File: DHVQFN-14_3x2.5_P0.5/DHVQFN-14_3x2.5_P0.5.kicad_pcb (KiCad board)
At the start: 2 copper layers, 20.3 x 22.9 mm, 6 parts, among them J101 Conn_01x09, J102 Conn_01x09, J103 Conn_01x12, J104 Conn_01x09, U101 DHVQFN-14

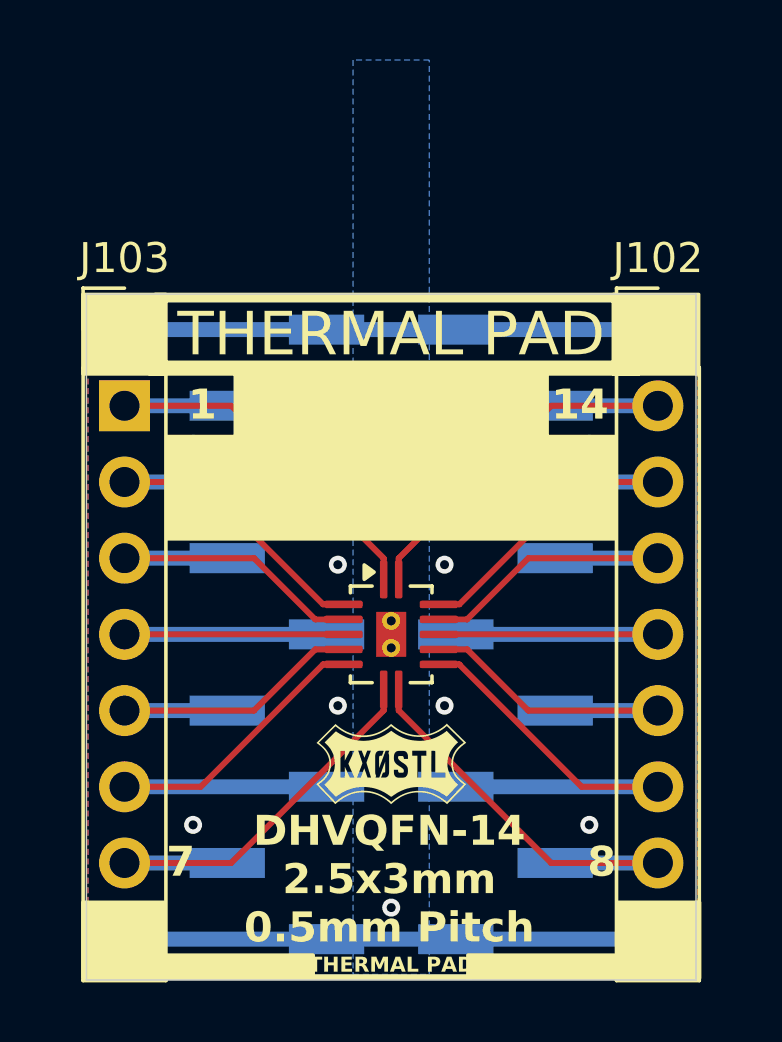
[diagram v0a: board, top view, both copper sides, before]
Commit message: Created SMDIP-16, QFP-48, QFP-32, QFN-80, QFN-68, QFN-64, QFN-60, QFN-56, QFN-48, QFN-36, QFN-28, QFN-20, QFP-32, QFP-48
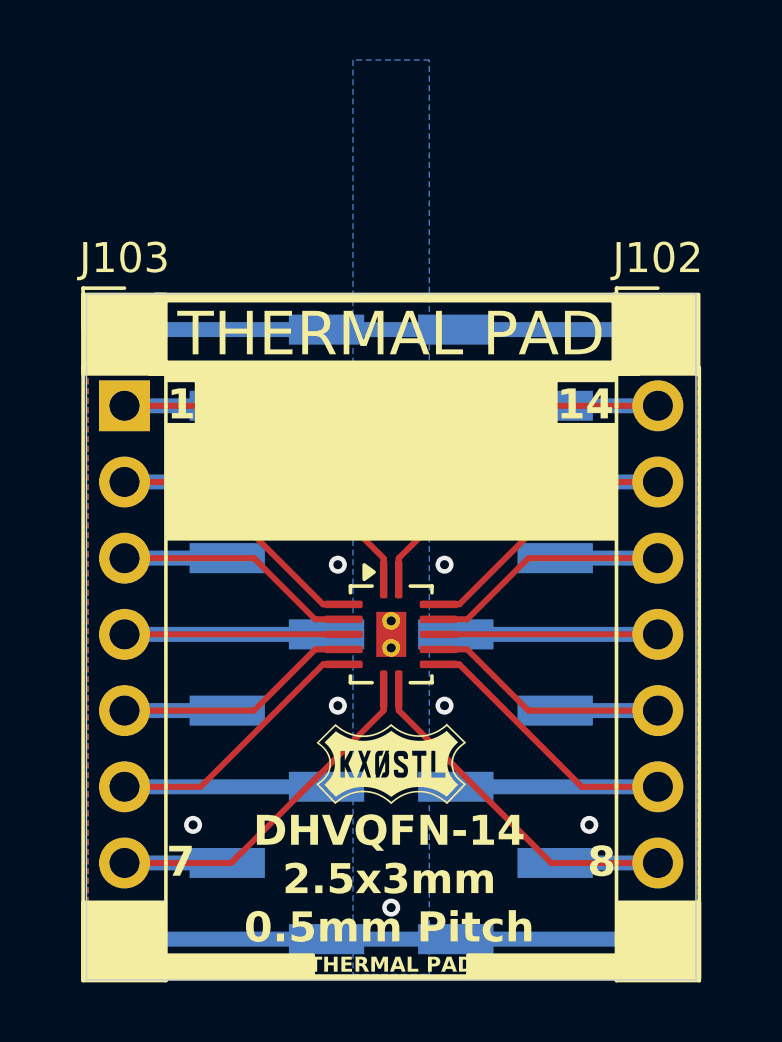
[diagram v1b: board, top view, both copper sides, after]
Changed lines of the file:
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@@
+	)
+	(gr_rect
+		(start 125.659 102.410557)
+		(end 140.533 102.795957)
+		(stroke
+			(width 0.1)
+			(type solid)
+		)
+		(fill yes)
+		(layer "F.SilkS")
 	)
 	(gr_rect
 		(start 130.302 122.630176)
 		(end 135.763 122.713037)
+		(stroke
+			(width 0.1)
+			(type solid)
+		)
+		(fill yes)
+		(layer "F.SilkS")
+	)
+	(gr_rect
+		(start 125.663 104.2545)
+		(end 140.537 107.2655)
 		(stroke
 			(width 0.1)
@@
 	)
 	(gr_rect
-		(start 127.889 102.489)
-		(end 138.303 106.68)
+		(start 126.599 102.489)
+		(end 138.593 106.68)
 		(stroke
 			(width 0.1)
@@
 	)
 	(gr_text "14"
-		(at 139.389 103.595274 0)
-		(layer "F.SilkS")
+		(at 139.57 103.59 0)
+		(layer "F.SilkS" knockout)
 		(effects
 			(font
@@
 	)
 	(gr_text "1"
-		(at 126.803 103.595274 0)
-		(layer "F.SilkS")
+		(at 126.1 103.59 0)
+		(layer "F.SilkS" knockout)
 		(effects
 			(font
